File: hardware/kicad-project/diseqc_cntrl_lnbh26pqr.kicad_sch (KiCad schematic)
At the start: 21 parts, among them IC5 LNBH26PQR, J6 SMA_Sock, J7 SMA_Sock

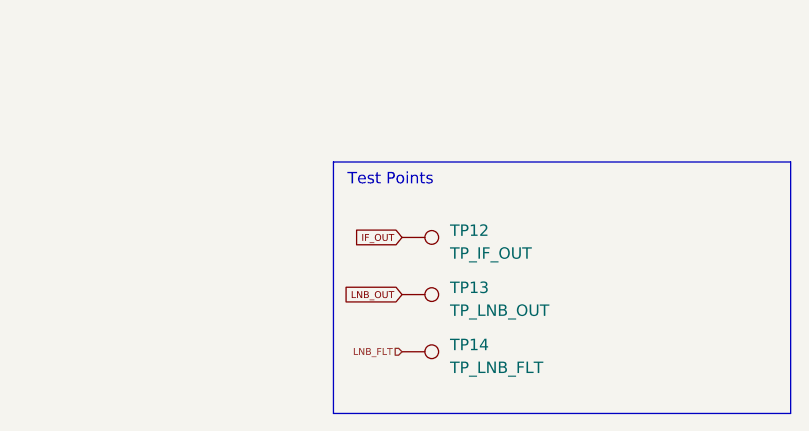
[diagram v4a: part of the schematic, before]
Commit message: Added test points for I2C1
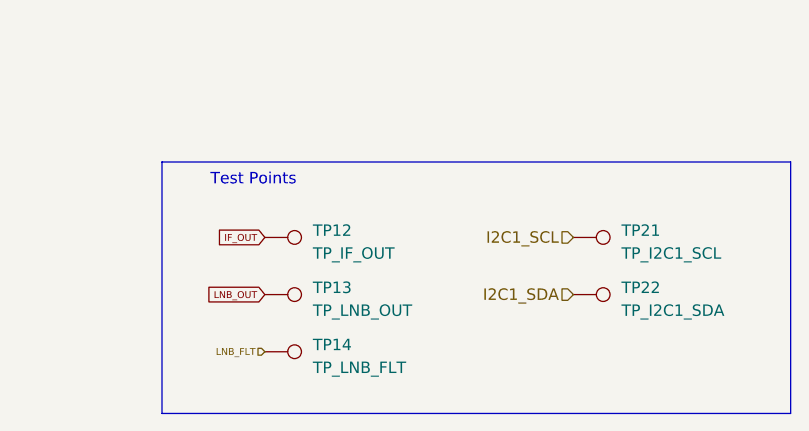
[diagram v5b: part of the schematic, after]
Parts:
- added TP21: TP_I2C1_SCL, TestPoint:TestPoint_THTPad_D1.0mm_Drill0.5mm, symbol Connector:TestPoint
- added TP22: TP_I2C1_SDA, TestPoint:TestPoint_THTPad_D1.0mm_Drill0.5mm, symbol Connector:TestPoint
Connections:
- net I2C1_SCL: now also TP21.1
- net I2C1_SDA: now also TP22.1
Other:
- moved on the sheet: TP12, TP13, TP14

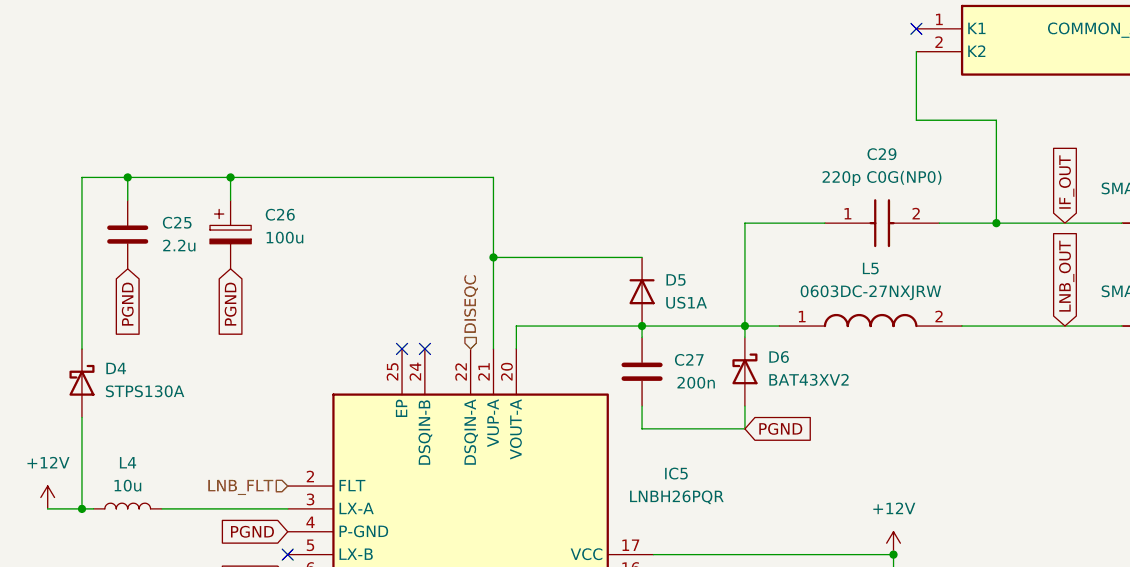
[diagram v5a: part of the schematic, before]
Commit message: Added InvenTree part codes
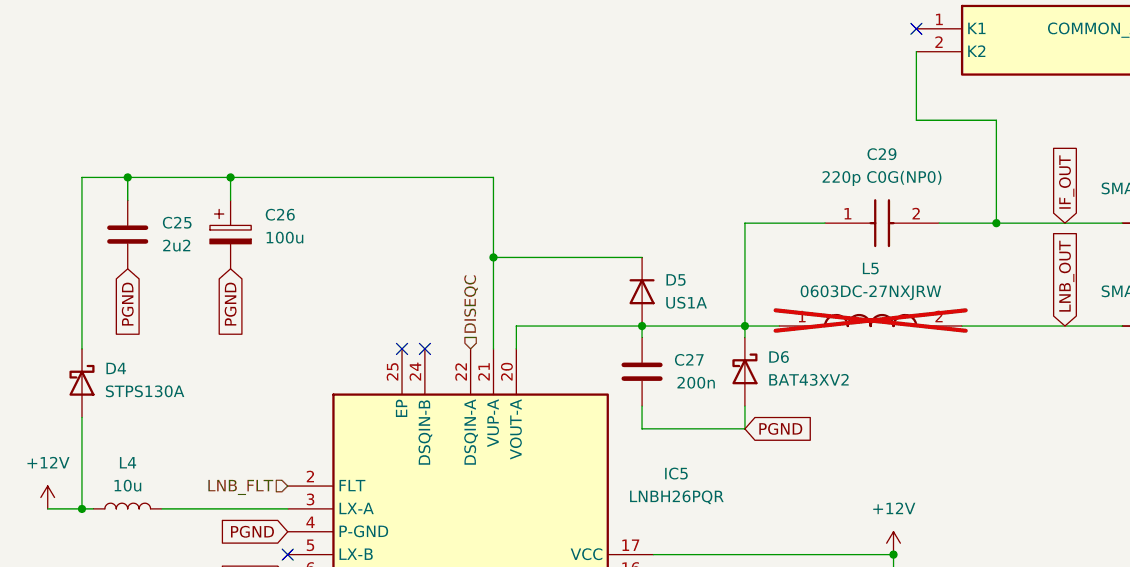
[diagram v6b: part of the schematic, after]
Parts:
- C24, C26: InvenTree (none) -> 91
- C25: value 2.2u -> 2u2; InvenTree (none) -> 71
- C27, C28, C30: InvenTree (none) -> 68
- C29: InvenTree (none) -> 70
- D4: InvenTree (none) -> 85
- D5: InvenTree (none) -> 103
- D6: InvenTree (none) -> 87
- D7: InvenTree (none) -> 86
- IC5: InvenTree (none) -> 124
- J6, J7: InvenTree (none) -> 81
- L4: InvenTree (none) -> 97
- L5: InvenTree (none) -> 98; now not fitted
- R16: InvenTree (none) -> 105

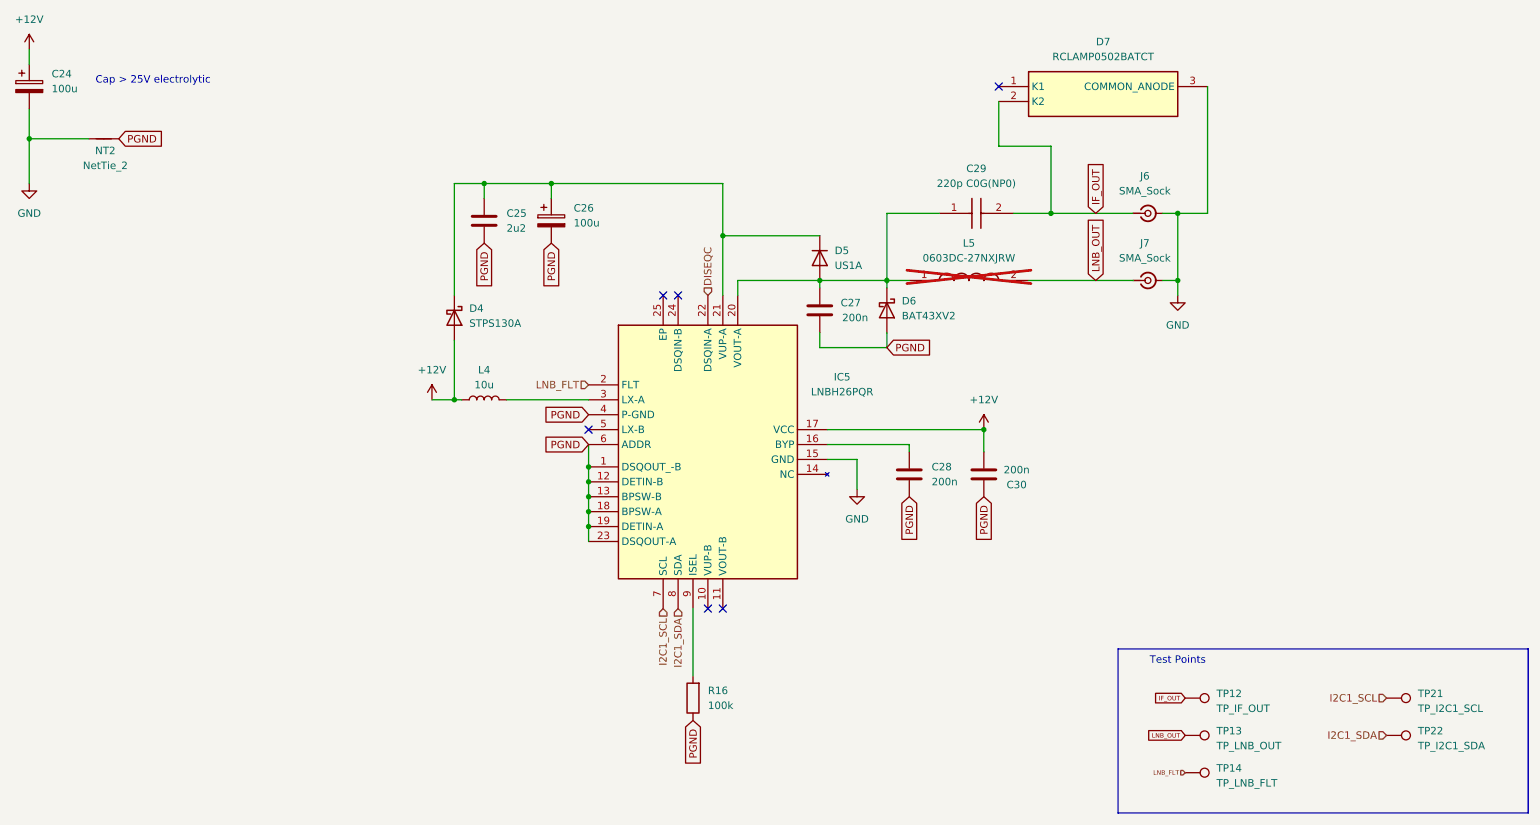
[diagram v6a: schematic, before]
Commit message: nwe board laylout for LAN8742A
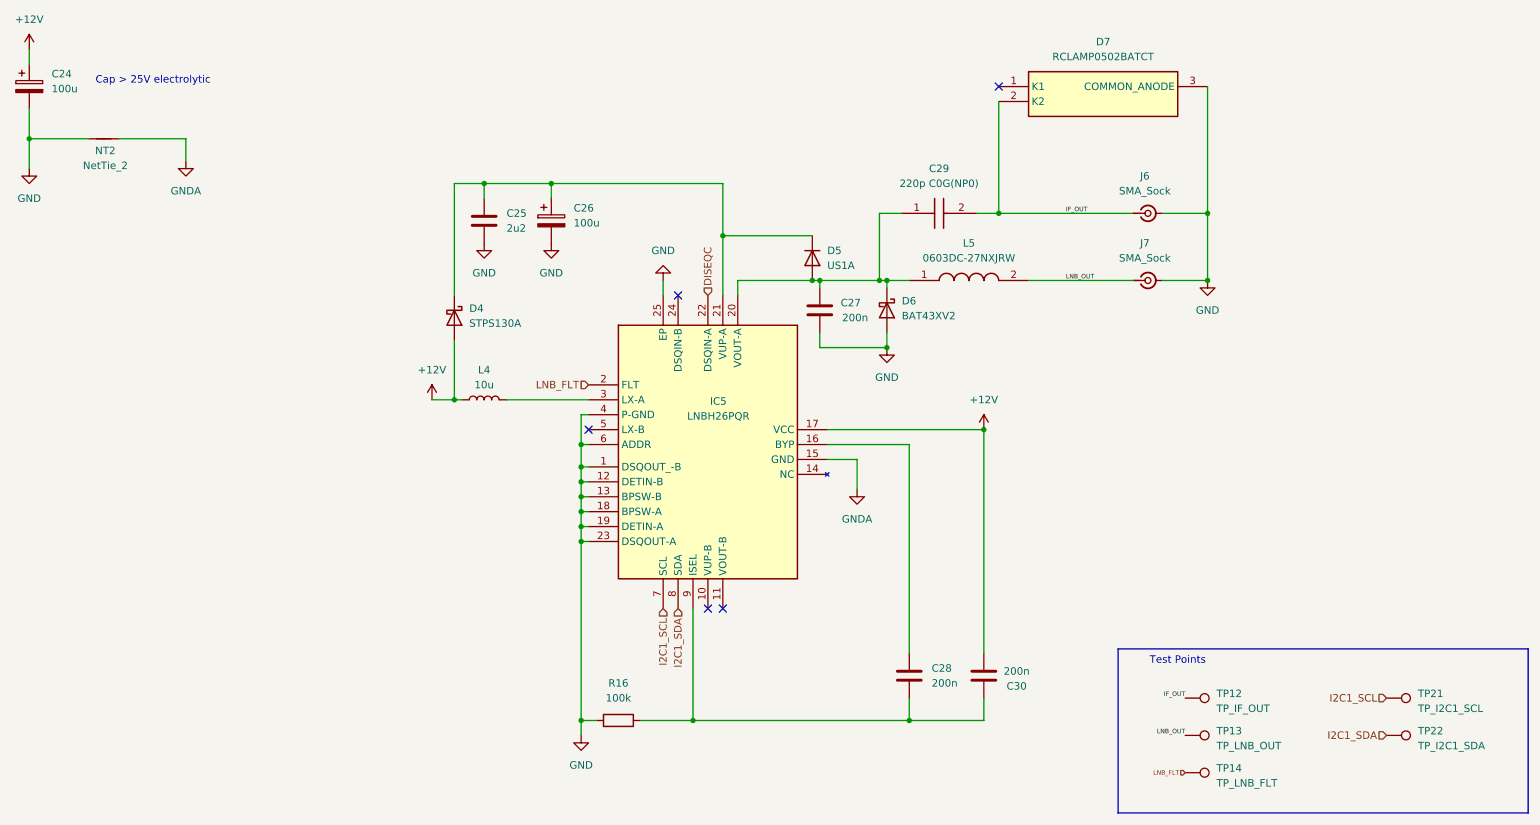
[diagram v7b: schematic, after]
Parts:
- L5: now fitted
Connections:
- net GND: now also C25.2, C26.2, C27.2, D6.2 (A), IC5.1 (DSQOUT_-B), IC5.12 (DETIN-B), IC5.13 (BPSW-B), IC5.18 (BPSW-A), IC5.19 (DETIN-A), IC5.23 (DSQOUT-A), IC5.25 (EP), IC5.4 (P-GND), IC5.6 (ADDR), R16.2; no longer IC5.15 (GND)
- net at IC5.9 (ISEL): now also C28.1, C30.1, R16.1; no longer R16.2
- removed net PGND: C25.2, C26.2, C27.2, C28.1, C30.1, D6.2 (A), IC5.1 (DSQOUT_-B), IC5.12 (DETIN-B), IC5.13 (BPSW-B), IC5.18 (BPSW-A), IC5.19 (DETIN-A), IC5.23 (DSQOUT-A), IC5.4 (P-GND), IC5.6 (ADDR), NT2.2, R16.1
- new net GNDA: IC5.15 (GND), NT2.2
- no-connect marks 6 -> 5
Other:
- moved on the sheet: C28, C29, C30, D5, R16

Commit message: Added MCU decoupling
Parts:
- renumbered C24 to C23, C25 to C24, C26 to C25, C27 to C26, C29 to C27, C30 to C29, L4 to L3, L5 to L4, R16 to R19, TP12 to TP10, TP13 to TP11, TP14 to TP12, TP21 to TP13, TP22 to TP14
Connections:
- net I2C1_SCL renamed SCL
- net I2C1_SDA renamed SDA
